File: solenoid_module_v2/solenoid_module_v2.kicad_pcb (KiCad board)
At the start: 2 copper layers, 35.5 x 21.8 mm, 17 parts, among them J1 1x5 2.54, J2 1x5 2.54, J5 1x3 5.08, Q1 BC817, SW1 3way switch, U1 TMCS1107A3, U2 ADS1115IDGS

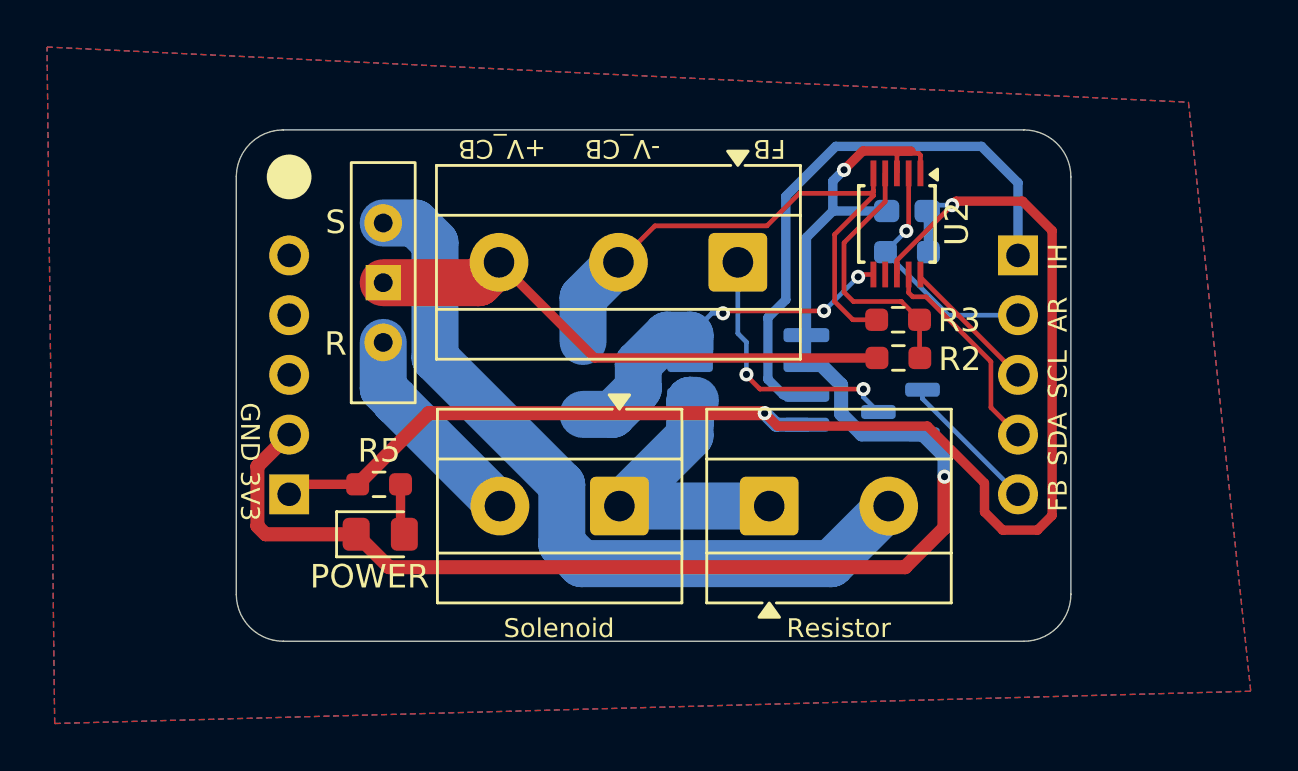
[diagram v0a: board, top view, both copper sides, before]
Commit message: Solenoid moduke new ver
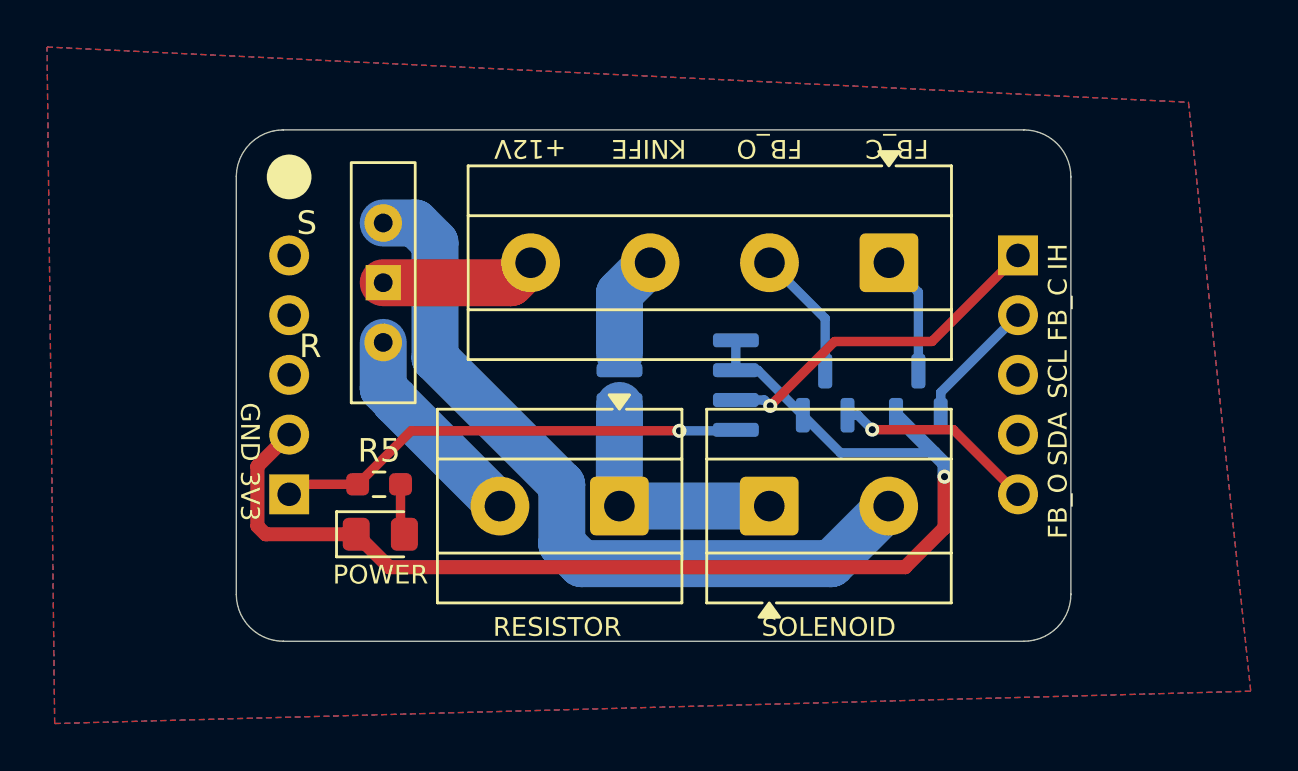
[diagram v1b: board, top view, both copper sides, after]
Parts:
- removed C1: 0.1 uF, Capacitor_SMD:C_0603_1608Metric_Pad1.08x0.95mm_HandSolder
- removed R1: R01, Resistor_SMD:R_1206_3216Metric_Pad1.30x1.75mm_HandSolder
- removed R2: 10K, Resistor_SMD:R_0603_1608Metric_Pad0.98x0.95mm_HandSolder
- removed R3: 3K3, Resistor_SMD:R_0603_1608Metric_Pad0.98x0.95mm_HandSolder
- removed R4: 10k, Resistor_SMD:R_0603_1608Metric_Pad0.98x0.95mm_HandSolder
- removed U2: ADS1115IDGS, Package_SO:TSSOP-10_3x3mm_P0.5mm
- added Q2: BC817, Package_TO_SOT_SMD:SOT-23, B.Cu at (82.8, 35.7)
- J5: value 1x3 5.08 -> 1x4 5.08; footprint TerminalBlock_MetzConnect:TerminalBlock_MetzConnect_Type101_RT01603HBWC_1x03_P5.08mm_Horizontal -> TerminalBlock_MetzConnect:TerminalBlock_MetzConnect_Type101_RT01604HBWC_1x04_P5.08mm_Horizontal
- moved J5 6.43 mm to (81.5, 30.1)
- moved Q1 3.30 mm to (78.8, 35.7), turned to 90 degrees
- moved U1 3.01 mm to (72.5, 35.4)
- renumbered POWER to D2, Resistor to J3, Solenoid to RESISTOR
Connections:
- J2 pad 2: /ADC/ALERT/READY -> Net-(J2-Pin_2)
- J5 pad 2: /ADC/A1 -> Net-(J5-Pin_2)
- J5 pad 3: +12V_camera_box -> /Current measure/IN-
- Q1 pad 3: Net-(J5-Pin_1) -> Net-(J5-Pin_2)
- U1 pad 3: /ADC/A2 -> /Current measure/IN-
- U1 pad 4: /ADC/A2 -> /Current measure/IN-
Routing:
- net +3V3: track 62.8 -> 20.1 mm, vias 2 -> 1
- net /ADC/A1: track 24.3 -> 0.00 mm
- net +12V_camera_box: track 23.0 -> 6.62 mm
- net /ADC/A2: track 16.0 -> 0.00 mm, vias 3 -> 0
- net GND: track 63.4 -> 51.9 mm, vias 2 -> 1
- net /ADC/A0: track 11.4 -> 0.00 mm
- net /ADC/ALERT/READY: track 10.5 -> 0.00 mm, vias 1 -> 0
- net /Current measure/I_Hall: track 24.5 -> 14.8 mm, vias 0 -> 1
- net SDA: track 9.07 -> 0.00 mm
- net Net-(J5-Pin_1): track 11.5 -> 5.13 mm, vias 2 -> 0
- net SCL: track 5.99 -> 0.00 mm
- net Net-(J2-Pin_2): track 0.00 -> 5.62 mm
- net Net-(J5-Pin_2): track 0.00 -> 5.59 mm
- net /Current measure/IN-: track 0.00 -> 4.41 mm
- net /Current measure/IN+: track 13.4 -> 10.7 mm
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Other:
- board text added: "+12V"
- board text added: "FB_C"
- board text added: "FB_O"
- board text added: "KNIFE"
- board text added: "POWER"
- board text added: "RESISTOR"
- board text added: "SOLENOID"
- board text added: "solenoid module v1.1.0"
- board text removed: "+V_CB"
- board text removed: "-V_CB"
- board text removed: "AR"
- board text removed: "FB"
- board text removed: "solenoid module v1.0.0"
